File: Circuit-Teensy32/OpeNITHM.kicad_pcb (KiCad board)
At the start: 2 copper layers, 100 x 45.3 mm, 25 parts, among them J1 Conn_01x14, J2 Conn_01x14, J7 Conn_02x12_Odd_Even, J8 Conn_02x12_Odd_Even, J9 Conn_01x05, U1 74HC4051, U2 74HC4051, U3 74HC4051, U4 74HC4051

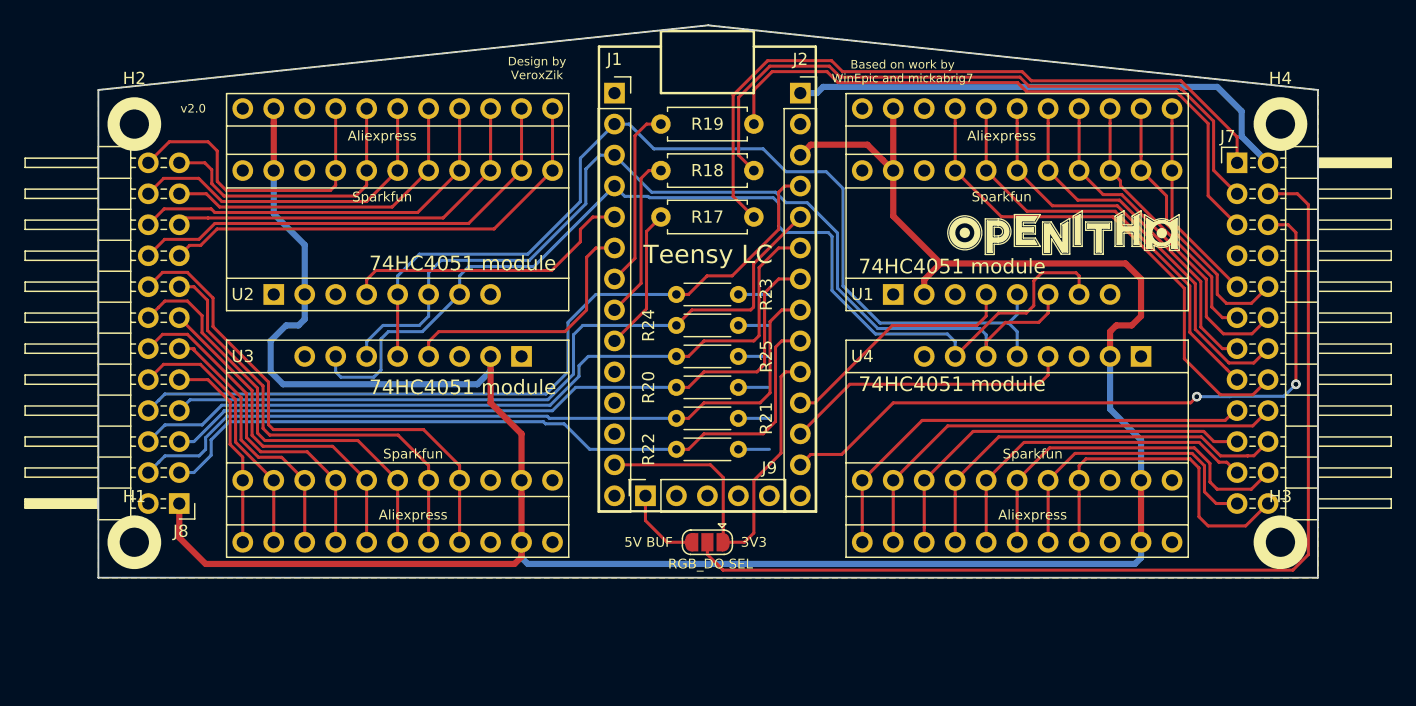
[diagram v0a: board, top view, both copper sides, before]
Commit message: Update 32 key board to v2.1
Reorganizes pins so DMA can be used, drops APA102 support, adds additional pins for complex IR LED boards.
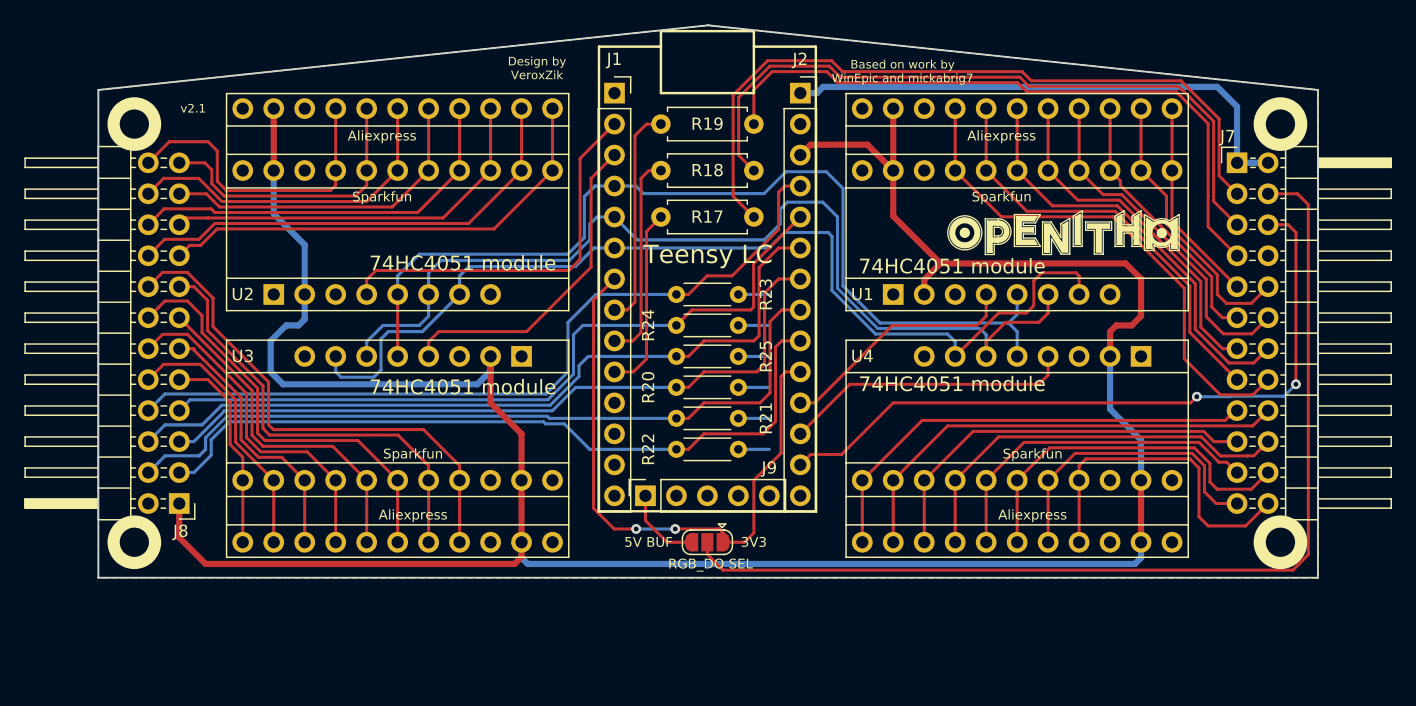
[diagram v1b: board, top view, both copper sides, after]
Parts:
- R20, R21, R22, R23, R24, R25: value 51k -> R_AIR
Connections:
- J1 pad 10: Net-(J1-Pad10) -> /LED_0
- J1 pad 13: /RGB_DO -> Net-(J1-Pad13)
- J1 pad 2: /MUX_0 -> /TOUCH_1
- J1 pad 3: /MUX_1 -> /TOUCH_2
- J1 pad 4: /MUX_2 -> /MUX_0
- J1 pad 5: /TOUCH_1 -> /MUX_1
- J1 pad 6: /TOUCH_2 -> /MUX_2
- J1 pad 7: /LED_2 -> /RGB_DO
- J1 pad 8: /LED_1 -> /LED_2
- J1 pad 9: /LED_0 -> /LED_1
- J2 pad 13: /RGB_CO -> Net-(J2-Pad13)
- J7 pad 1: /LED_0_OUT -> +5V
- J7 pad 3: /LED_1_OUT -> /LED_0_OUT
- J7 pad 5: /LED_2_OUT -> /LED_1_OUT
- J7 pad 6: /RGB_CO -> GND
- J7 pad 7: Net-(J7-Pad7) -> /LED_2_OUT
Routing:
- net /RGB_DO: track 33.0 -> 50.1 mm, vias 0 -> 2
- net /TOUCH_1: track 24.2 -> 31.7 mm
- net /TOUCH_2: track 22.2 -> 27.0 mm
- net /MUX_2: track 87.2 -> 82.9 mm
- net /LED_0: track 11.7 -> 15.2 mm
- net /LED_1: track 13.6 -> 17.0 mm
- net /LED_2: track 15.0 -> 18.1 mm
- net /MUX_0: track 81.0 -> 78.2 mm
- net /LED_1_OUT: track 55.1 -> 57.7 mm
- net /LED_0_OUT: track 57.9 -> 60.4 mm
- net /LED_2_OUT: track 51.7 -> 54.3 mm
- net +5V: track 42.4 -> 43.8 mm
- net /MUX_1: track 81.4 -> 80.3 mm
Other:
- board text added: "v2.1"
- board text removed: "v2.0"

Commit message: Changes to v2.1
Broke out all spare pins to Teensy,
No more solder jumper for RGB data line,
Added solder jumper for IR LED power option (+5v by default)
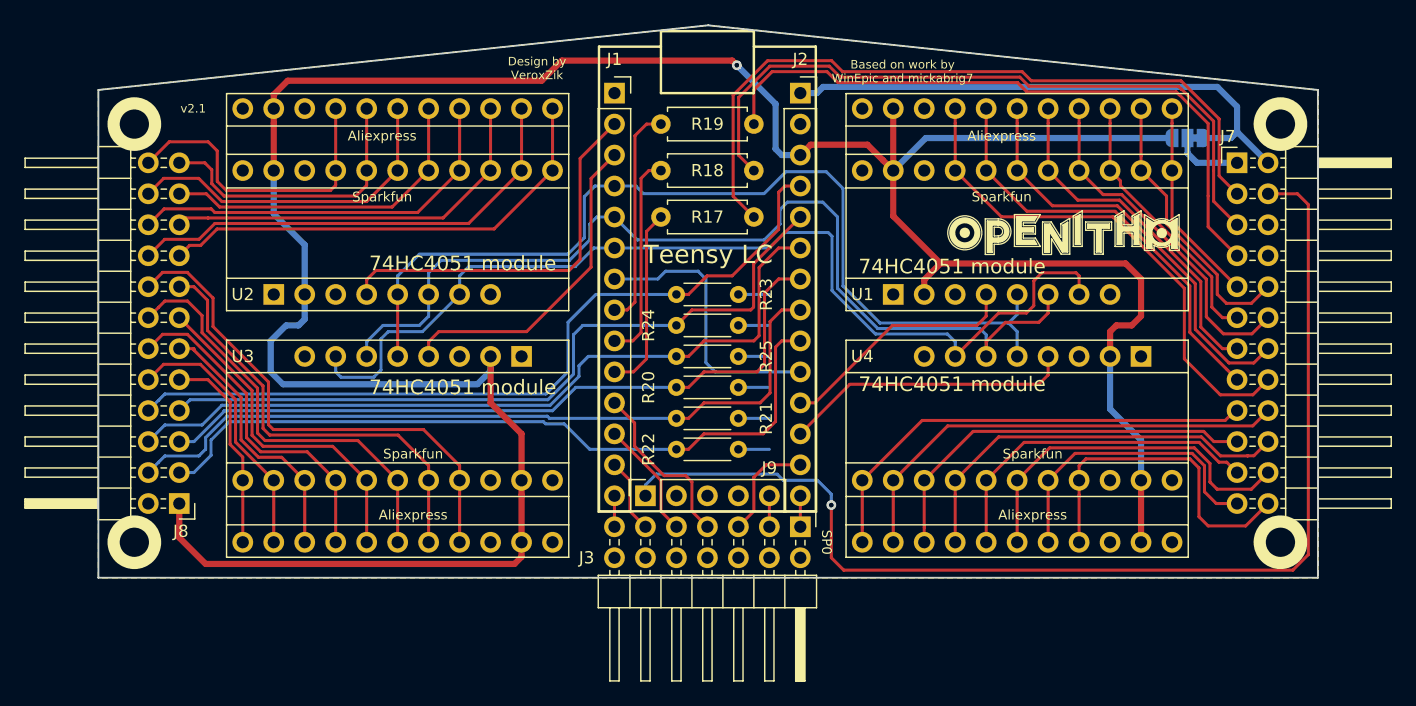
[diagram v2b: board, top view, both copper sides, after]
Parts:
- added J3: Conn_02x07_Odd_Even, Connector_PinHeader_2.54mm:PinHeader_2x07_P2.54mm_Horizontal, F.Cu at (162.6, 83.8)
- JP1: value SolderJumper_3_Open -> SolderJumper_3_Bridged12; footprint Jumper:SolderJumper-3_P1.3mm_Open_RoundedPad1.0x1.5mm -> Jumper:SolderJumper-3_P1.3mm_Bridged12_RoundedPad1.0x1.5mm; moved to B.Cu
- moved JP1 51.5 mm to (194.3, 51.9)
- moved LOGO2 27.3 mm to (180.2, 74.7)
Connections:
- J1 pad 11: Net-(J1-Pad11) -> /SPARE_3
- J1 pad 12: Net-(J1-Pad12) -> /SPARE_4
- J1 pad 13: Net-(J1-Pad13) -> /SPARE_5
- J1 pad 14: Net-(J1-Pad14) -> /SPARE_6
- J2 pad 13: Net-(J2-Pad13) -> /SPARE_2
- J2 pad 14: Net-(J2-Pad14) -> /SPARE_0
- J7 pad 1: +5V -> VCC
- J7 pad 4: /RGB_DO_OUT -> /RGB_DO_BUF
- J9 pad 5: Net-(J9-Pad5) -> /SPARE_1
- JP1 pad 1: /RGB_DO -> +5V
- JP1 pad 2: /RGB_DO_OUT -> VCC
- JP1 pad 3: /RGB_DO_BUF -> +3V3
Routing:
- net /RGB_DO_BUF: track 6.55 -> 94.8 mm, vias 0 -> 1
- net /RGB_DO_OUT: track 83.7 -> 0.00 mm
- net /RGB_CO: track 58.4 -> 0.00 mm, vias 2 -> 0
- net /RGB_DO: track 50.1 -> 22.9 mm, vias 2 -> 0
- net +3V3: track 215.4 -> 236.4 mm, vias 0 -> 1
- net /SPARE_3: track 0.00 -> 14.4 mm
- net /SPARE_4: track 0.00 -> 9.72 mm
- net /SPARE_2: track 0.00 -> 8.82 mm
- net /SPARE_5: track 0.00 -> 6.13 mm
- net VCC: track 0.00 -> 5.64 mm
- net /SPARE_6: track 0.00 -> 2.54 mm
- net /SPARE_1: track 0.00 -> 2.54 mm
- net /SPARE_0: track 0.00 -> 2.54 mm
- net +5V: track 43.8 -> 45.3 mm
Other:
- board text added: "J3 (Bottom of Board)"
- board text added: "SP0"
- board text added: "SP1"
- board text added: "SP2"
- board text added: "SP3"
- board text added: "SP4"
- board text added: "SP5"
- board text added: "SP6"
- board text removed: "5V BUF"
- board text removed: "RGB_DO SEL"
